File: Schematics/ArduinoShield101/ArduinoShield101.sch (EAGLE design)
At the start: 18 parts, among them IC1 INA122U

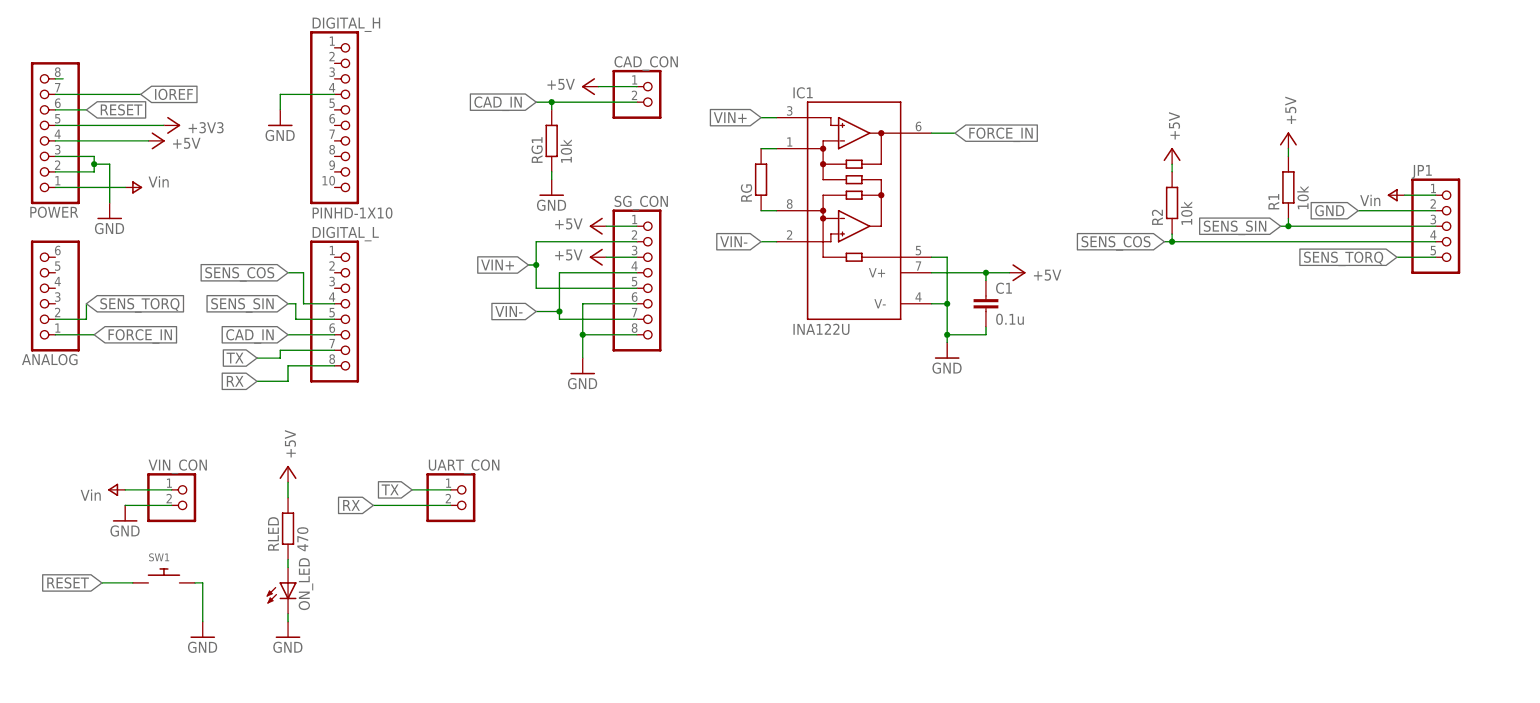
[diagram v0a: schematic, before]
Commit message: Updated Arduino Shield to the version that was printed.
Includes CAM files.
Some changes must be made to the Shield to ease mounting/soldering.
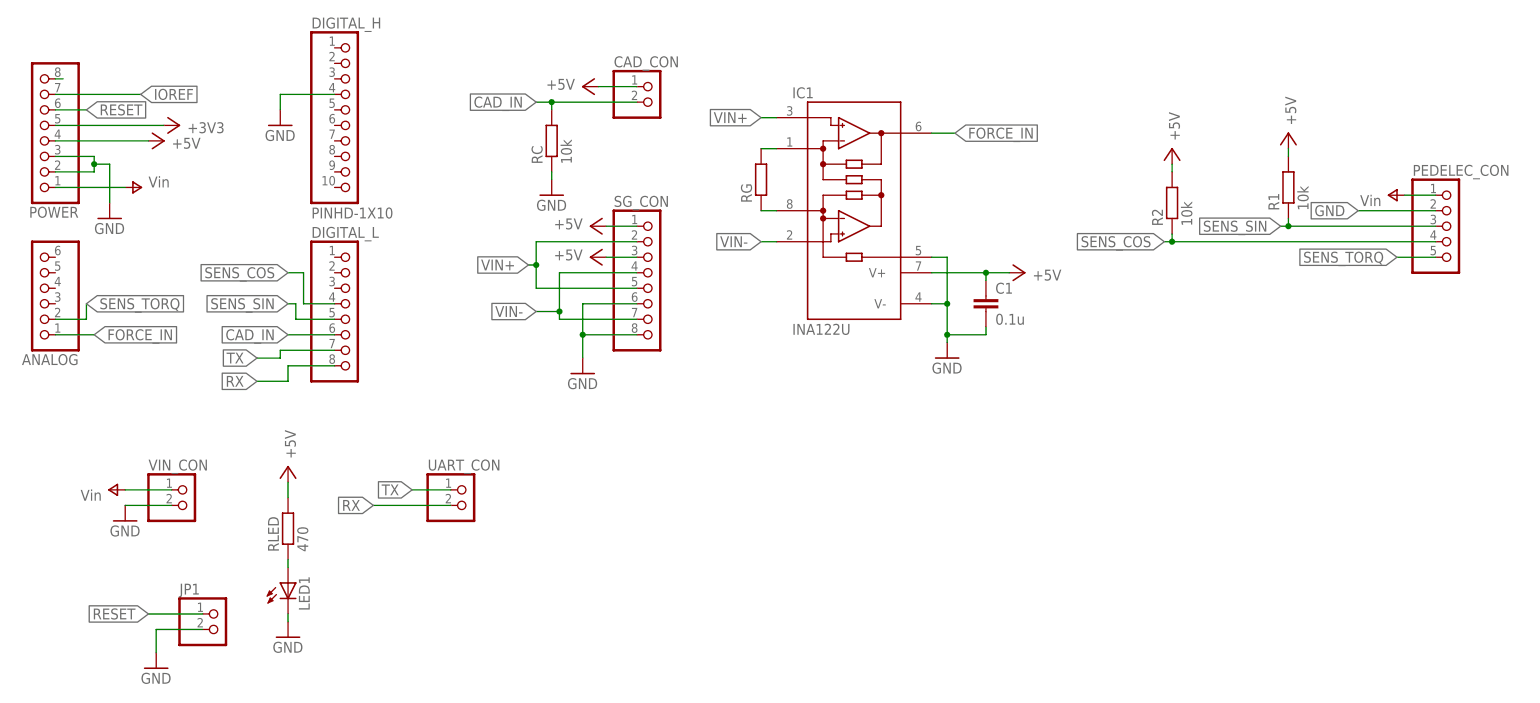
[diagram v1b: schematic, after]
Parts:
- removed ON_LED: (no value), adafruit:LED3MM
- removed RG1: 10k, rcl:R-EU_0207/5V
- removed SW1: (no value), adafruit:SWITCH_PUSHBUTTONC&K_KSS
- added LED1: (no value), adafruit:LEDCHIPLED_0603
- added PEDELEC_CON: (no value), pinhead:PINHD-1X5/90
- added RC: 10k, rcl:R-EU_R0603
- C1: device rcl:C-EU025-024X044 -> rcl:C-EUC0603
- JP1: device pinhead:PINHD-1X5/90 -> pinhead:PINHD-1X2
- R1, R2, RG, RLED: device rcl:R-EU_0207/5V -> rcl:R-EU_R0603
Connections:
- net CAD_IN: now also RC.2; no longer RG1.2
- net GND: now also LED1.C, PEDELEC_CON.2, RC.1; no longer ON_LED.C, RG1.1, SW1.P$2
- net N$4: now also LED1.A; no longer ON_LED.A
- net RESET: now also JP1.1; no longer SW1.P$1
- net SENS_COS: now also PEDELEC_CON.4; no longer JP1.4
- net SENS_SIN: now also PEDELEC_CON.3; no longer JP1.3
- net SENS_TORQ: now also PEDELEC_CON.5; no longer JP1.5
- net V+: now also PEDELEC_CON.1; no longer JP1.1
